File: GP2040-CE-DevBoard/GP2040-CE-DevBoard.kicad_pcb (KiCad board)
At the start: 2 copper layers, 137.8 x 68.6 mm, 50 parts, among them J1 USB_C_Receptacle, J2 Conn_02x22_Odd_Even, J3 Debug, J4 RGB LED, SW1 Up, SW10 4k, SW11 1P, SW12 2P, SW13 3P, SW14 4P, SW15 BOOTSEL, SW16 Settings, SW17 LSB, SW18 RSB, SW19 Home, SW2 Down, SW20 Reset, SW21 TP, SW3 Left, SW4 Right, SW5 Select, SW6 Start, SW7 1k, SW8 2k, SW9 3k, U1 Raspbery Pi Pico, U2 ADS1219IPWR, U3 ADS1219IPWR, U4 Left Stick, U5 Right Stick

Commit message: Restarting PCB design
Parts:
- added RV1: 10k, Potentiometer_THT:Potentiometer_Vishay_148-149_Single_Horizontal, F.Cu at (-71.5, 45.7)
- added RV2: 10k, Potentiometer_THT:Potentiometer_Vishay_148-149_Single_Horizontal, F.Cu at (-55.6, -12.2)
- R1, R3, R4, U1: moved to F.Cu
- moved R5 232.2 mm to (-73.6, 83.8)
- moved C5 225.0 mm to (-64.0, 64.6)
- moved C4 224.8 mm to (-64.0, 67.6)
- moved U2 224.5 mm to (-71.2, 74.5)
- moved SW6 223.7 mm to (-57.1, 5.84)
- moved SW19 223.1 mm to (-68.6, 0.76)
- moved SW7 216.4 mm to (-21.4, 18.7)
- moved C3 212.7 mm to (-64.0, 61.6), turned to 0 degrees
- moved U5 208.9 mm to (-11.7, -11.8)
- moved SW18 206.0 mm to (-17.8, 6.60)
- moved C1 199.3 mm to (-73.6, 80.8)
- moved SW10 197.4 mm to (-36.2, 34.0)
- moved U4 196.5 mm to (-29.3, -11.8)
- moved U3 192.6 mm to (-71.2, 64.9)
- moved C2 187.9 mm to (-59.2, 61.6)
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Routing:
- net GND: track 753.6 -> 0.00 mm, vias 40 -> 0
- net Left: track 166.9 -> 0.00 mm, vias 6 -> 0
- net TP: track 163.4 -> 0.00 mm, vias 9 -> 0
- net Up: track 157.9 -> 0.00 mm, vias 4 -> 0
- net Down: track 153.6 -> 0.00 mm, vias 8 -> 0
- net +3V3: track 137.5 -> 0.00 mm, vias 2 -> 0
- net Right: track 136.8 -> 0.00 mm, vias 3 -> 0
- net 4P: track 134.9 -> 0.00 mm, vias 4 -> 0
- net LSB: track 134.3 -> 0.00 mm, vias 5 -> 0
- net BOOTSEL: track 134.2 -> 0.00 mm, vias 4 -> 0
- net SETTINGS: track 133.8 -> 0.00 mm, vias 5 -> 0
- net 3P: track 118.3 -> 0.00 mm, vias 7 -> 0
- net Select: track 103.6 -> 0.00 mm, vias 5 -> 0
- net RUN: track 100.9 -> 0.00 mm, vias 5 -> 0
- net RGB: track 92.3 -> 0.00 mm, vias 3 -> 0
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- removed copper zone on B.Cu, net GND
- removed copper zone on F.Cu, net GND
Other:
- board size 137.8 x 68.6 mm -> 145 x 61 mm

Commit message: Updating schema and PCB design
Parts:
- removed SW20: Reset, Button_Switch_SMD:SW_Push_1P1T_NO_6x6mm_H9.5mm
- removed SW21: TP, Button_Switch_SMD:SW_Push_1P1T_NO_6x6mm_H9.5mm
- added J5: qwiic, Connector_JST:JST_SH_BM04B-SRSS-TB_1x04-1MP_P1.00mm_Vertical, F.Cu at (199.1, 71.9)
- C1, C2, C3, C4, C5, C6, R3, R4, U1, U2, U3: moved to B.Cu
- D1, D2, D3, D4: footprint LED_SMD:LED_0805_2012Metric_Pad1.15x1.40mm_HandSolder -> ul_ADS1219IPWR:LED_0805_2012Metric_Pad1.15x1.40mm_HandSolder
- R1, R2, R5, R6: footprint Resistor_SMD:R_0805_2012Metric_Pad1.20x1.40mm_HandSolder -> ul_ADS1219IPWR:R_0805_2012Metric_Pad1.20x1.40mm_HandSolder; moved to B.Cu
- R10, R7, R8, R9: footprint Resistor_SMD:R_0805_2012Metric_Pad1.20x1.40mm_HandSolder -> ul_ADS1219IPWR:R_0805_2012Metric_Pad1.20x1.40mm_HandSolder
- RV1, RV2: footprint Potentiometer_THT:Potentiometer_Vishay_148-149_Single_Horizontal -> Connector_PinHeader_2.54mm:PinHeader_1x03_P2.54mm_Vertical
- SW10: value 4k -> L2
- SW11: value 1P -> B3
- SW12: value 2P -> B4
- SW13: value 3P -> R1
- SW14: value 4P -> L1
- SW17: value LSB -> A1
- SW18: value RSB -> Reset
- SW19: value Home -> A2
- SW5: value Select -> S1
- SW6: value Start -> S2
- SW7: value 1k -> B1
- SW8: value 2k -> B2
- SW9: value 3k -> R2
- moved RV2 255.0 mm to (182.6, 78.7), turned to 90 degrees
- moved U2 238.1 mm to (163.1, 116.8), turned to 180 degrees
- moved R5 236.5 mm to (161.0, 113.0)
- moved SW19 236.5 mm to (149.0, 93.5)
- moved SW13 234.7 mm to (175.8, 87.4)
- moved SW7 234.1 mm to (192.8, 113.1)
- moved C5 227.1 mm to (157.0, 117.1), turned to 180 degrees
- moved C4 226.0 mm to (157.0, 115.1), turned to 180 degrees
- moved C6 223.0 mm to (157.0, 119.1), turned to 180 degrees
- moved U5 216.8 mm to (162.4, 117.3)
- moved SW9 216.2 mm to (175.8, 80.3)
- moved SW6 213.4 mm to (134.4, 100.1)
- moved U3 210.6 mm to (132.8, 116.8), turned to 180 degrees
- moved U4 207.5 mm to (133.2, 117.3)
- moved SW17 207.1 mm to (149.0, 100.1)
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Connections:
- J2 pad 11: Start -> B2
- J2 pad 13: 1K -> B3
- J2 pad 15: 2K -> B4
- J2 pad 17: 3K -> L1
- J2 pad 19: 4K -> R1
- J2 pad 21: LSB -> L2
- J2 pad 23: L3 -> R2
- J2 pad 25: RSB -> S1
- J2 pad 27: R3 -> S2
- J2 pad 29: SETTINGS -> L3
- J2 pad 31: 1P -> R3
- J2 pad 33: 2P -> A1
- J2 pad 35: 3P -> A2
- J2 pad 37: 4P -> BOOTSEL
- J2 pad 39: BOOTSEL -> RUN
- J2 pad 41: Home -> (no net)
- J2 pad 42: GND -> (no net)
- J2 pad 43: TP -> (no net)
- J2 pad 44: GND -> (no net)
- J2 pad 9: Select -> B1
- SW10 pad 1: 4K -> L2
- SW11 pad 1: 1P -> B3
- SW12 pad 1: 2P -> B4
- SW13 pad 1: 3P -> R1
- SW14 pad 1: 4P -> L1
- SW17 pad 1: LSB -> A1
- SW18 pad 1: RSB -> RUN
- SW19 pad 1: Home -> A2
- SW5 pad 1: Select -> S1
- SW6 pad 1: Start -> S2
- SW7 pad 1: 1K -> B1
- SW8 pad 1: 2K -> B2
- SW9 pad 1: 3K -> R2
- U1 pad 1: Left -> PLED1
- U1 pad 10: 1P -> B2
- U1 pad 11: 2P -> R2
- U1 pad 12: 3P -> L2
- U1 pad 14: 4P -> B3
- U1 pad 15: 1K -> B4
- U1 pad 16: 2K -> R1
- U1 pad 17: 3K -> L1
- U1 pad 19: 4K -> PLED3
- U1 pad 2: Up -> PLED2
- U1 pad 20: RGB -> PLED4
- U1 pad 21: PLED1 -> S1
- U1 pad 22: PLED2 -> S2
- U1 pad 24: PLED3 -> L3
- U1 pad 25: PLED4 -> R3
- U1 pad 26: TP -> A1
- U1 pad 27: LSB -> A2
- U1 pad 29: RSB -> RGB
- U1 pad 4: Down -> Up
- U1 pad 5: Right -> Down
- U1 pad 6: Home -> Right
- U1 pad 7: Select -> Left
- U1 pad 9: Start -> B1
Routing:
- net Up: track 0.00 -> 151.9 mm, vias 0 -> 2
- net B3: track 0.00 -> 144.8 mm, vias 0 -> 2
- net Left: track 0.00 -> 143.7 mm, vias 0 -> 3
- net Down: track 0.00 -> 137.6 mm, vias 0 -> 2
- net L1: track 0.00 -> 128.3 mm, vias 0 -> 6
- net B2: track 0.00 -> 121.1 mm, vias 0 -> 1
- net B1: track 0.00 -> 114.7 mm
- net Right: track 0.00 -> 109.8 mm, vias 0 -> 2
- net R2: track 0.00 -> 99.9 mm, vias 0 -> 2
- net D-: track 0.00 -> 80.0 mm, vias 0 -> 4
- net D+: track 0.00 -> 78.9 mm, vias 0 -> 4
- net B4: track 0.00 -> 77.6 mm, vias 0 -> 1
- net L2: track 0.00 -> 75.7 mm, vias 0 -> 2
- net R1: track 0.00 -> 66.3 mm, vias 0 -> 2
- net RUN: track 0.00 -> 65.0 mm, vias 0 -> 1
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- added copper zone on B.Cu, net GND
- added copper zone on F.Cu, net GND
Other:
- board text added: "GND"
- board text added: "SWCLK"

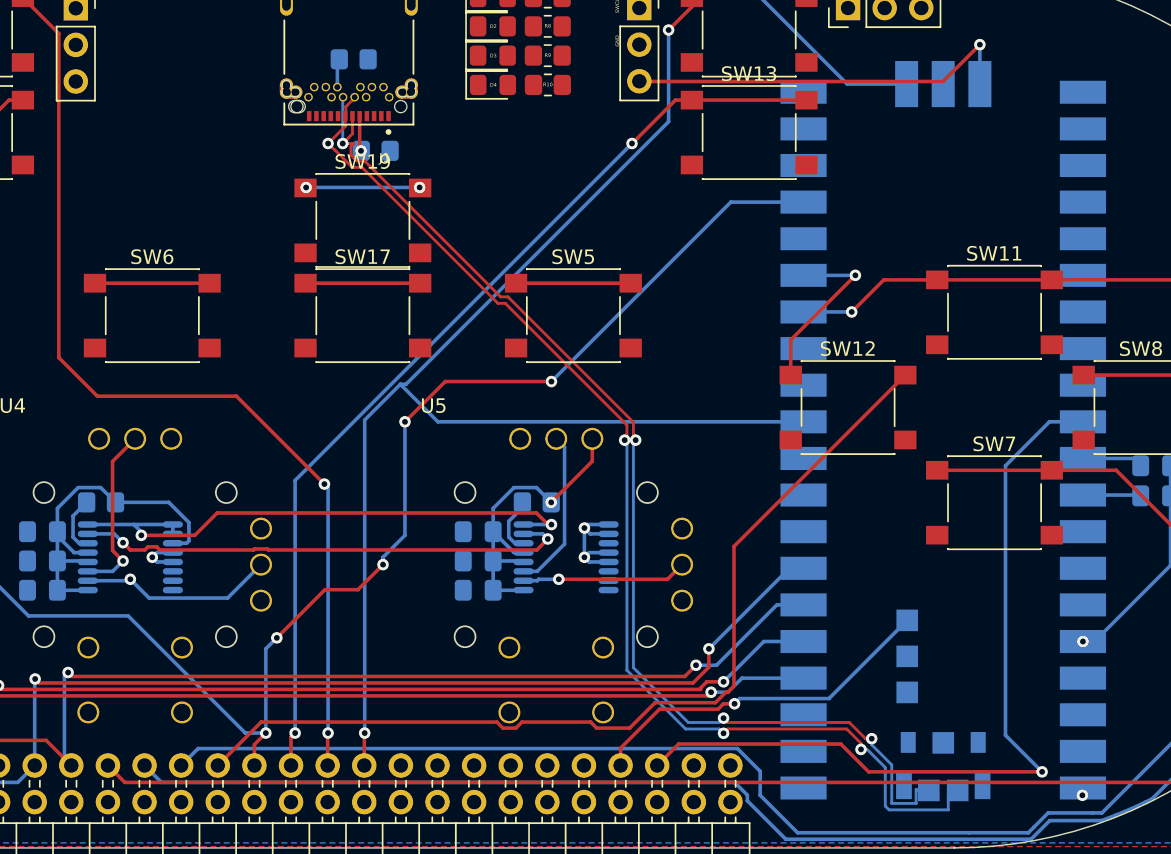
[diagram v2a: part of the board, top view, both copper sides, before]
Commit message: routing by hand is a pain
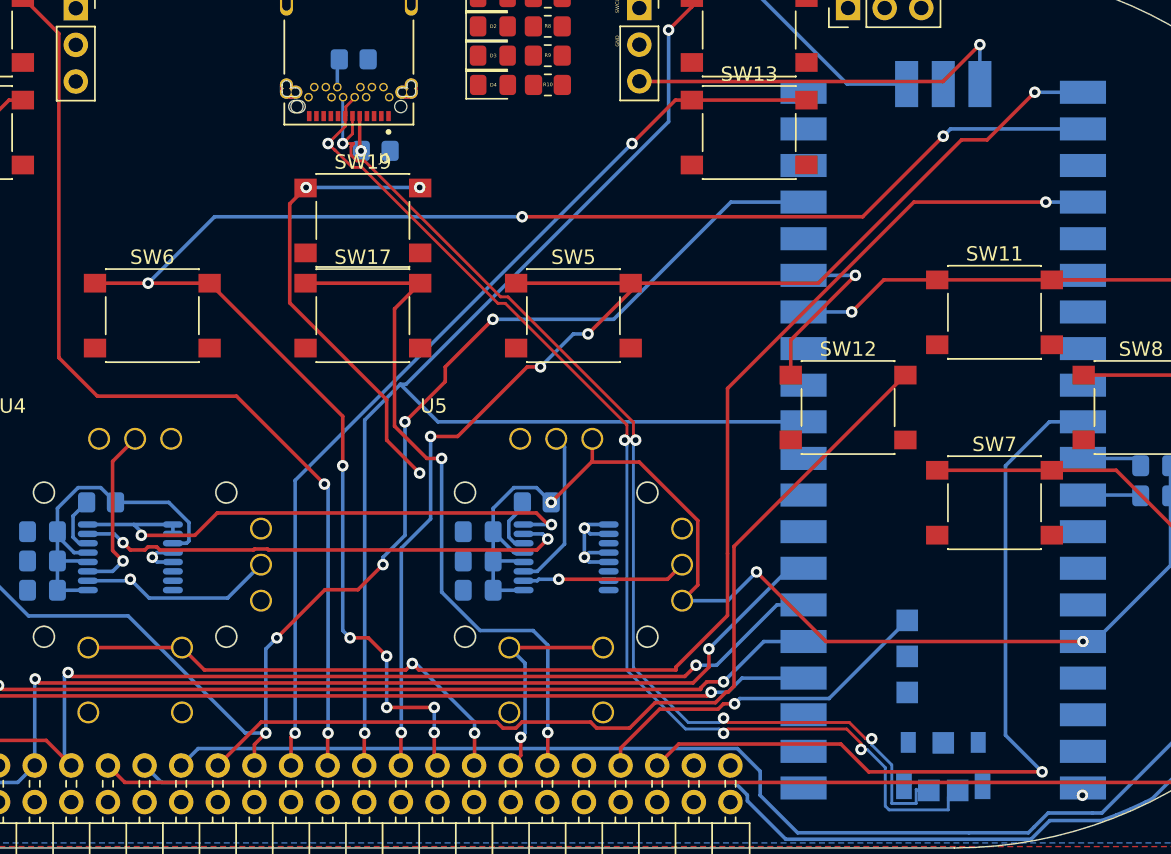
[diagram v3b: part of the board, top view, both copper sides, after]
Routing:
- net S2: track 7.95 -> 119.9 mm, vias 0 -> 9
- net L3: track 0.00 -> 101.8 mm, vias 0 -> 3
- net S1: track 7.95 -> 87.1 mm, vias 0 -> 5
- net +3V3: track 63.9 -> 109.6 mm, vias 2 -> 3
- net A1: track 7.95 -> 49.3 mm, vias 0 -> 2
- net A2: track 7.87 -> 31.9 mm, vias 2 -> 3
- net R3: track 0.00 -> 15.5 mm, vias 0 -> 1
- net L1: track 128.3 -> 128.9 mm

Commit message: Nearly finished!
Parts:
- C1, C2, C3, C4, C5, C6, R3, R4: footprint Capacitor_SMD:C_0805_2012Metric_Pad1.18x1.45mm_HandSolder -> ul_NCP1117DT33T5G:C_0805_2012Metric_Pad1.18x1.45mm_HandSolder
- J5: moved to B.Cu
- moved J5 41.0 mm to (211.6, 111.0), turned to 90 degrees
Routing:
- net +3V3: track 109.6 -> 269.7 mm, vias 3 -> 12
- net SETTINGS: track 7.95 -> 131.3 mm, vias 0 -> 5
- net VBUS: track 0.00 -> 121.4 mm, vias 1 -> 7
- net BOOTSEL: track 32.7 -> 121.5 mm, vias 1 -> 7
- net A2: track 31.9 -> 114.7 mm, vias 3 -> 9
- net RGB: track 0.00 -> 82.8 mm, vias 0 -> 6
- net PLED2: track 0.00 -> 80.3 mm, vias 0 -> 5
- net R3: track 15.5 -> 95.1 mm, vias 1 -> 6
- net RUN: track 65.0 -> 144.2 mm, vias 1 -> 7
- net PLED1: track 0.00 -> 72.6 mm, vias 0 -> 5
- net GND: track 12.4 -> 83.4 mm, vias 3 -> 26
- net LSB2: track 0.00 -> 62.9 mm, vias 0 -> 2
- net SDA: track 39.0 -> 97.8 mm, vias 2 -> 5
- net RSB2: track 0.00 -> 55.0 mm, vias 0 -> 7
- net SCL: track 42.9 -> 97.3 mm, vias 2 -> 9
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
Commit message: Progress
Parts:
- removed RV1, RV2: 10k, Connector_PinHeader_2.54mm:PinHeader_1x03_P2.54mm_Vertical
- removed SW1: Up, Button_Switch_SMD:SW_Push_1P1T_NO_6x6mm_H9.5mm
- removed SW10: L2, Button_Switch_SMD:SW_Push_1P1T_NO_6x6mm_H9.5mm
- removed SW11: B3, Button_Switch_SMD:SW_Push_1P1T_NO_6x6mm_H9.5mm
- removed SW12: B4, Button_Switch_SMD:SW_Push_1P1T_NO_6x6mm_H9.5mm
- removed SW13: R1, Button_Switch_SMD:SW_Push_1P1T_NO_6x6mm_H9.5mm
- removed SW14: L1, Button_Switch_SMD:SW_Push_1P1T_NO_6x6mm_H9.5mm
- removed SW15: BOOTSEL, Button_Switch_SMD:SW_Push_1P1T_NO_6x6mm_H9.5mm
- removed SW16: Settings, Button_Switch_SMD:SW_Push_1P1T_NO_6x6mm_H9.5mm
- removed SW17: A1, Button_Switch_SMD:SW_Push_1P1T_NO_6x6mm_H9.5mm
- removed SW18: Reset, Button_Switch_SMD:SW_Push_1P1T_NO_6x6mm_H9.5mm
- removed SW19: A2, Button_Switch_SMD:SW_Push_1P1T_NO_6x6mm_H9.5mm
- removed SW2: Down, Button_Switch_SMD:SW_Push_1P1T_NO_6x6mm_H9.5mm
- removed SW3: Left, Button_Switch_SMD:SW_Push_1P1T_NO_6x6mm_H9.5mm
- removed SW4: Right, Button_Switch_SMD:SW_Push_1P1T_NO_6x6mm_H9.5mm
- removed SW5: S1, Button_Switch_SMD:SW_Push_1P1T_NO_6x6mm_H9.5mm
- removed SW6: S2, Button_Switch_SMD:SW_Push_1P1T_NO_6x6mm_H9.5mm
- removed SW7: B1, Button_Switch_SMD:SW_Push_1P1T_NO_6x6mm_H9.5mm
- removed SW8: B2, Button_Switch_SMD:SW_Push_1P1T_NO_6x6mm_H9.5mm
- removed SW9: R2, Button_Switch_SMD:SW_Push_1P1T_NO_6x6mm_H9.5mm
- removed U4: Left Stick, THB001P:THB001P
- removed U5: Right Stick, THB001P:THB001P
- added REF**: MountingHole_2.5mm, MountingHole:MountingHole_2.5mm, F.Cu at (143.5, 126.5)
- added REF**: MountingHole_2.5mm, MountingHole:MountingHole_2.5mm, F.Cu at (105.9, 52.8)
- added REF**: MountingHole_2.5mm, MountingHole:MountingHole_2.5mm, F.Cu at (112.3, 126.2)
- added REF**: MountingHole_2.5mm, MountingHole:MountingHole_2.5mm, F.Cu at (143.3, 52.8)
- C1, C2, C3, C4, C5, C6, R3, R4: footprint ul_NCP1117DT33T5G:C_0805_2012Metric_Pad1.18x1.45mm_HandSolder -> OpenStick:C_0805_2012Metric_Pad1.18x1.45mm_HandSolder; moved to F.Cu
- D1, D2, D3, D4: footprint ul_ADS1219IPWR:LED_0805_2012Metric_Pad1.15x1.40mm_HandSolder -> OpenStick:LED_0805_2012Metric_Pad1.15x1.40mm_HandSolder
- J1: footprint UJ31-CH-31-SMT-TR:CUI_UJ31-CH-31-SMT-TR -> Connector_USB:USB_C_Receptacle_GCT_USB4085
- J2: value Conn_02x22_Odd_Even -> Conn_02x21_Odd_Even; footprint Connector_PinSocket_2.54mm:PinSocket_2x22_P2.54mm_Horizontal -> Connector_PinHeader_2.54mm:PinHeader_2x21_P2.54mm_Vertical
- J3, J4: footprint Connector_PinSocket_2.54mm:PinSocket_1x03_P2.54mm_Vertical -> Connector_PinHeader_2.54mm:PinHeader_1x03_P2.54mm_Vertical
- J5: footprint Connector_JST:JST_SH_BM04B-SRSS-TB_1x04-1MP_P1.00mm_Vertical -> Connector_JST:JST_SH_SM04B-SRSS-TB_1x04-1MP_P1.00mm_Horizontal; moved to F.Cu
- R1, R2, R5, R6: footprint ul_ADS1219IPWR:R_0805_2012Metric_Pad1.20x1.40mm_HandSolder -> OpenStick:R_0805_2012Metric_Pad1.20x1.40mm_HandSolder; moved to F.Cu
- R10, R7, R8, R9: footprint ul_ADS1219IPWR:R_0805_2012Metric_Pad1.20x1.40mm_HandSolder -> OpenStick:R_0805_2012Metric_Pad1.20x1.40mm_HandSolder
- U1: footprint ul_SC0915:SC0915 -> OpenStick:Raspberry Pi Pico - pogo pin and screw mount; moved to F.Cu
- U2, U3: footprint ul_ADS1219IPWR:ADS1219IPWR -> OpenStick:ADS1219IPWR; moved to F.Cu
- moved R4 78.9 mm to (129.3, 87.3), turned to 90 degrees
- moved J5 70.4 mm to (143.8, 91.9)
- moved R3 67.8 mm to (138.9, 91.2), turned to 90 degrees
- moved J3 62.1 mm to (123.7, 122.1), turned to 90 degrees
- moved R10 60.0 mm to (107.7, 58.1), turned to 90 degrees
- moved R9 57.5 mm to (106.9, 65.0), turned to 180 degrees
- moved J2 56.9 mm to (104.9, 76.7), turned to 0 degrees
- moved D4 55.0 mm to (107.7, 62.0), turned to 90 degrees
- moved U1 53.6 mm to (136.7, 119.2)
- moved D1 51.0 mm to (110.7, 58.9)
- moved R7 51.0 mm to (114.5, 58.9)
- moved D3 50.2 mm to (110.7, 65.0), turned to 180 degrees
- moved R8 50.1 mm to (113.8, 65.8), turned to -90 degrees
- moved D2 47.7 mm to (113.8, 62.0), turned to -90 degrees
- moved C5 45.0 mm to (123.2, 87.3), turned to 90 degrees
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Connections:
- J2 pad 1: Up -> GND
- J2 pad 10: GND -> Right
- J2 pad 11: B2 -> GND
- J2 pad 12: GND -> Left
- J2 pad 13: B3 -> GND
- J2 pad 14: GND -> B1
- J2 pad 15: B4 -> GND
- J2 pad 16: GND -> B2
- J2 pad 17: L1 -> GND
- J2 pad 18: GND -> R2
- J2 pad 19: R1 -> GND
- J2 pad 2: GND -> SETTINGS
- J2 pad 20: GND -> L2
- J2 pad 21: L2 -> GND
- J2 pad 22: GND -> B3
- J2 pad 23: R2 -> GND
- J2 pad 24: GND -> B4
- J2 pad 25: S1 -> GND
- J2 pad 26: GND -> R1
- J2 pad 27: S2 -> GND
- J2 pad 28: GND -> L1
- J2 pad 29: L3 -> GND
- J2 pad 3: Down -> GND
- J2 pad 30: GND -> RUN
- J2 pad 31: R3 -> GND
- J2 pad 32: GND -> A2
- J2 pad 33: A1 -> GND
- J2 pad 34: GND -> A1
- J2 pad 35: A2 -> GND
- J2 pad 36: GND -> R3
- J2 pad 37: BOOTSEL -> GND
- J2 pad 38: GND -> L3
- J2 pad 39: RUN -> GND
- J2 pad 4: GND -> BOOTSEL
- J2 pad 40: GND -> S2
- J2 pad 41: (no net) -> GND
- J2 pad 42: (no net) -> S1
- J2 pad 5: Left -> GND
- J2 pad 6: GND -> Up
- J2 pad 7: Right -> GND
- J2 pad 8: GND -> Down
- J2 pad 9: B1 -> GND
- U1 pad 10: B2 -> Left
- U1 pad 11: R2 -> B1
- U1 pad 12: L2 -> B2
- U1 pad 14: B3 -> R2
- U1 pad 15: B4 -> L2
- U1 pad 16: R1 -> B3
- U1 pad 17: L1 -> B4
- U1 pad 19: PLED3 -> R1
- U1 pad 20: PLED4 -> L1
- U1 pad 4: Up -> PLED3
- U1 pad 5: Down -> PLED4
- U1 pad 6: Right -> Up
- U1 pad 7: Left -> Down
- U1 pad 9: B1 -> Right
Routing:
- net +3V3: track 269.7 -> 110.6 mm, vias 12 -> 3
- net Up: track 151.9 -> 9.22 mm, vias 2 -> 0
- net B3: track 144.8 -> 11.4 mm, vias 2 -> 0
- net Left: track 143.7 -> 10.3 mm, vias 3 -> 0
- net B2: track 142.6 -> 10.3 mm, vias 4 -> 0
- net Down: track 137.6 -> 9.22 mm, vias 2 -> 0
- net L1: track 128.6 -> 13.4 mm, vias 6 -> 0
- net B1: track 124.8 -> 10.3 mm, vias 1 -> 0
- net RUN: track 144.2 -> 35.6 mm, vias 7 -> 1
- net BOOTSEL: track 121.5 -> 17.0 mm, vias 7 -> 0
- net L2: track 114.7 -> 11.4 mm, vias 3 -> 0
- net Right: track 109.8 -> 10.3 mm, vias 2 -> 0
- net SETTINGS: track 131.3 -> 31.8 mm, vias 5 -> 1
- net S2: track 129.1 -> 35.1 mm, vias 9 -> 0
- net R2: track 103.6 -> 11.4 mm, vias 2 -> 0
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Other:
- board size 145 x 61 mm -> 44.4 x 79.9 mm
- board text removed: "GND"
- board text removed: "SWCLK"

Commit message: a lot of Silkscreen work
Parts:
- removed REF** (x4): MountingHole_2.5mm, MountingHole:MountingHole_2.5mm
- added J6: Conn_02x21_Odd_Even, Connector_PinHeader_2.54mm:PinHeader_2x21_P2.54mm_Vertical, F.Cu at (104.9, 76.7)
- added J7: Debug, Connector_PinSocket_2.54mm:PinSocket_1x03_P2.54mm_Vertical, F.Cu at (123.7, 122.2)
- added J8: RGB LED, Connector_PinSocket_2.54mm:PinSocket_1x03_P2.54mm_Vertical, F.Cu at (140.2, 69.6)
- added J9: qwiic, Connector_JST:JST_SH_SM04B-SRSS-TB_1x04-1MP_P1.00mm_Horizontal, F.Cu at (143.8, 91.9)
- J2: value Conn_02x21_Odd_Even -> Conn_01x04; footprint Connector_PinHeader_2.54mm:PinHeader_2x21_P2.54mm_Vertical -> Connector_PinHeader_2.54mm:PinHeader_1x05_P2.54mm_Vertical
- J3: value Debug -> Conn_01x03
- J4: value RGB LED -> Conn_01x04; footprint Connector_PinHeader_2.54mm:PinHeader_1x03_P2.54mm_Vertical -> Connector_PinHeader_2.54mm:PinHeader_1x05_P2.54mm_Vertical
- J5: value qwiic -> Conn_01x03; footprint Connector_JST:JST_SH_SM04B-SRSS-TB_1x04-1MP_P1.00mm_Horizontal -> Connector_PinHeader_2.54mm:PinHeader_1x03_P2.54mm_Vertical
- moved J2 48.7 mm to (139.7, 110.7)
- moved J4 41.3 mm to (143.5, 110.7)
- moved J3 26.6 mm to (139.7, 100.8), turned to 0 degrees
- moved J5 8.89 mm to (143.5, 100.8), turned to 0 degrees
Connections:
- J2 pad 1: GND -> +3V3
- J2 pad 2: SETTINGS -> RSX
- J2 pad 3: GND -> RSY
- J2 pad 4: BOOTSEL -> R3
- J3 pad 1: SWCLK -> +3V3
- J3 pad 2: GND -> RSB2
- J3 pad 3: SWDIO -> GND
- J4 pad 1: VBUS -> +3V3
- J4 pad 2: RGB -> LSX
- J4 pad 3: GND -> LSY
- J5 pad 1: SCL -> +3V3
- J5 pad 2: SDA -> LSB2
- J5 pad 3: +3V3 -> GND
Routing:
- net LSY: track 0.00 -> 42.1 mm, vias 0 -> 3
- net LSX: track 0.00 -> 39.6 mm, vias 0 -> 3
- net LSB2: track 0.00 -> 32.3 mm, vias 0 -> 2
- net +3V3: track 110.6 -> 137.0 mm
- net RSB2: track 0.00 -> 20.4 mm, vias 0 -> 1
- net RSX: track 0.00 -> 19.3 mm, vias 0 -> 1
- net RSY: track 0.00 -> 18.1 mm
- net R3: track 33.5 -> 48.3 mm
- net L3: track 33.5 -> 46.7 mm
- net GND: track 10.6 -> 19.9 mm, vias 0 -> 2
- net RUN: track 35.6 -> 39.5 mm
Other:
- board size 44.4 x 79.9 mm -> 44.4 x 76.9 mm
- board text added: "3V3"
- board text added: "3v3"
- board text added: "A1"
- board text added: "A2"
- board text added: "B1"
- board text added: "B2"
- board text added: "B3"
- board text added: "B4"
- board text added: "Boot Select"
- board text added: "Down"
- board text added: "GND"
- board text added: "L1"
- board text added: "L2"
- board text added: "L3"
- board text added: "LSX"
- board text added: "LSY"
- board text added: "LT"
- board text added: "Left"
- board text added: "R1"
- board text added: "R2"
- board text added: "R3"
- board text added: "RGB"
- board text added: "RSX"
- board text added: "RSY"
- board text added: "RT"
- board text added: "Right"
- board text added: "Run"
- board text added: "S1"
- board text added: "S2"
- board text added: "Settings"
- board text added: "Up"
- board text added: "VBUS"
